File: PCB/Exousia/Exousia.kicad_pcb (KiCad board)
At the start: 2 copper layers, 72 parts, among them J1 IN/out, J2 I2C buss, J3 in/OUT, Q1 2N7002, Q2 2N7002, Q3 2N7002, U1 AON7410, U2 AON7410, U3 RVSPG, U4 AON7410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

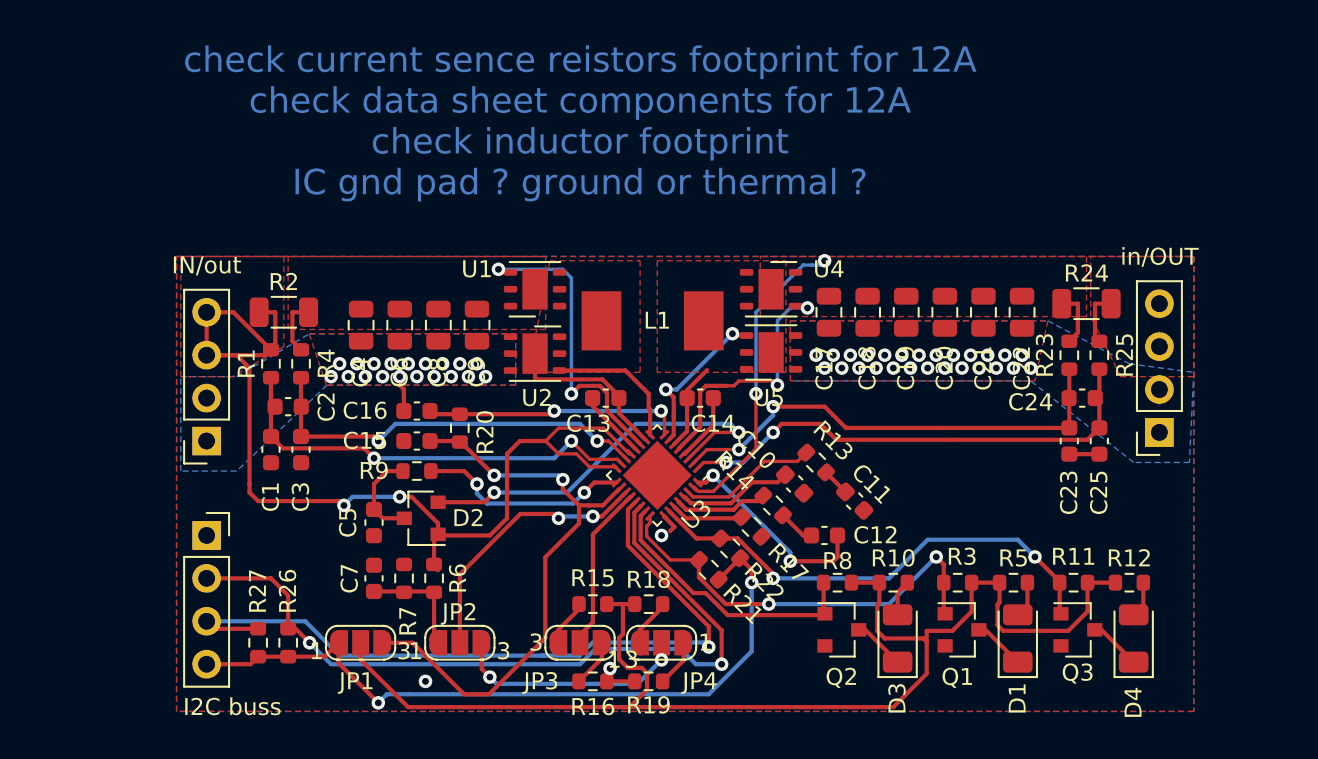
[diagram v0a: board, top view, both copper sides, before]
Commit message: upgraded sens resitors to handle 12A max. and retrouted a bit
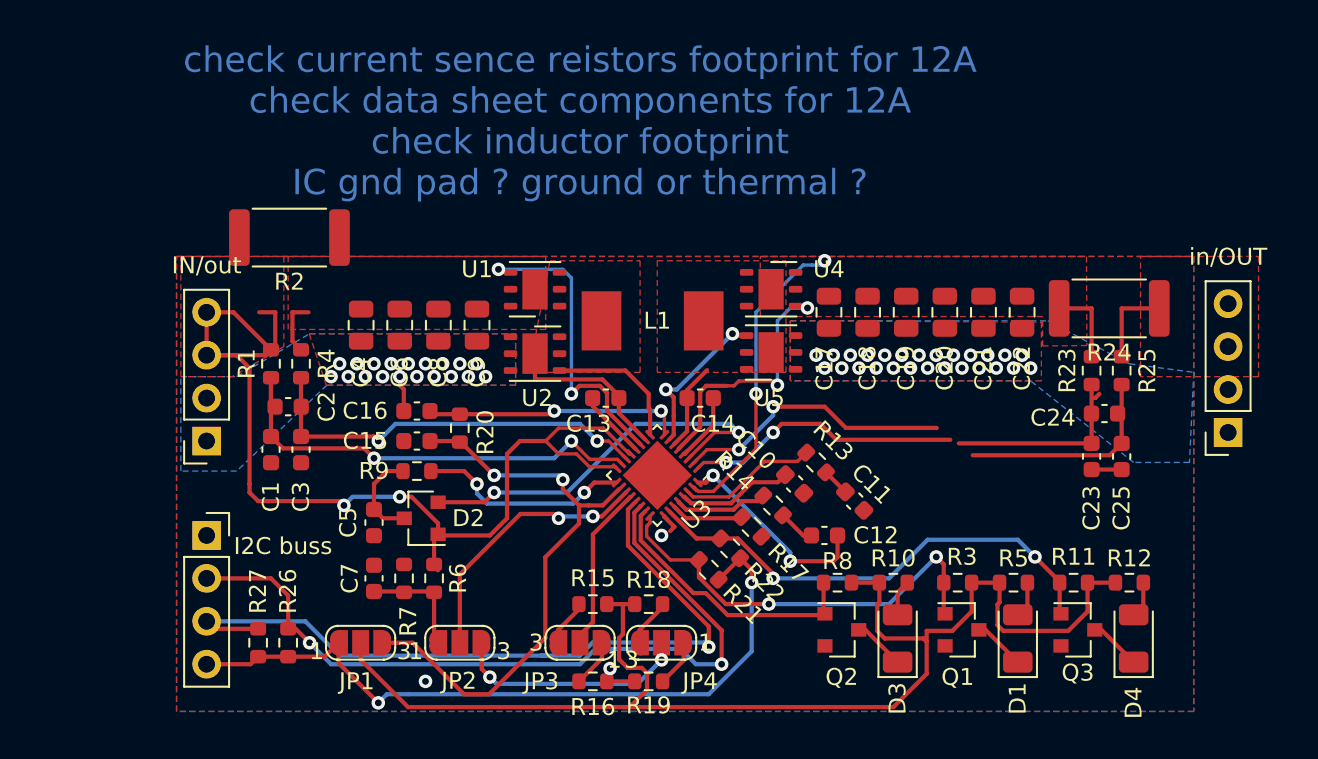
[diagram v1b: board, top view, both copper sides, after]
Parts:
- R2: value 0.02R -> 0.005R; footprint Resistor_SMD:R_1206_3216Metric -> Resistor_SMD:R_2512_6332Metric
- R24: value 0.01R -> 0.005R; footprint Resistor_SMD:R_1206_3216Metric -> Resistor_SMD:R_2512_6332Metric
- moved R2 4.43 mm to (138.3, 141.9)
- moved J3 4.06 mm to (193.8, 153.4)
- moved C25 1.61 mm to (187.5, 154.8)
- moved R25 1.61 mm to (187.5, 149.8)
- moved C23 1.61 mm to (185.7, 154.8)
- moved C24 1.61 mm to (186.5, 152.3)
- moved R23 1.61 mm to (185.7, 149.8)
- moved R24 1.37 mm to (186.8, 146.1)
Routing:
- net Net-(J3-Pad3): track 3.28 -> 5.08 mm
- net Net-(C17-Pad1): track 21.7 -> 23.1 mm

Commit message: improved the controle cirtitry for controleing the IC
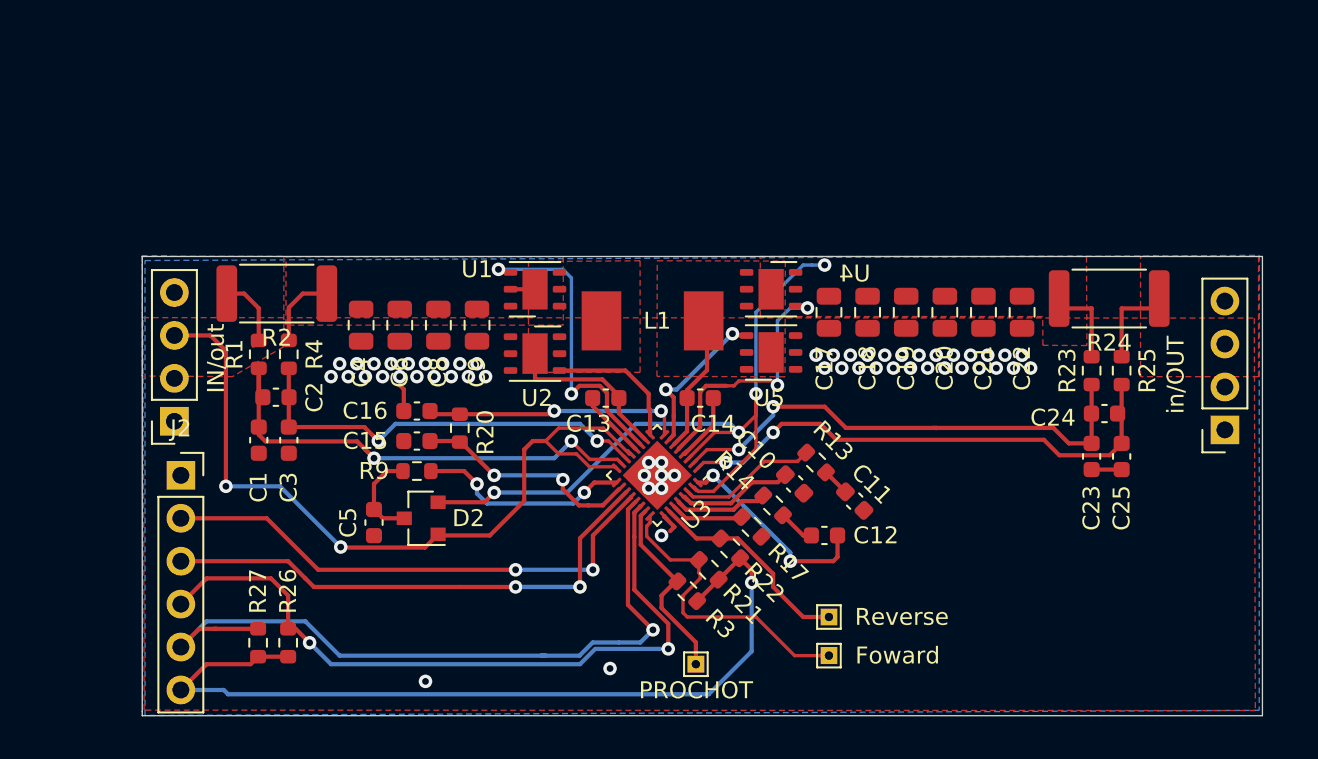
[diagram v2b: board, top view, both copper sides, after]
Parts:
- removed C7: 0.1uF, Capacitor_SMD:C_0603_1608Metric
- removed D1, D3: FRWPG, LED_SMD:LED_1206_3216Metric
- removed D4: RVSPG, LED_SMD:LED_1206_3216Metric
- removed JP1: IO-Vselect, Jumper:SolderJumper-3_P1.3mm_Open_RoundedPad1.0x1.5mm_NumberLabels
- removed JP2: Pin_FRWEN / ADP, Jumper:SolderJumper-3_P1.3mm_Open_RoundedPad1.0x1.5mm_NumberLabels
- removed JP3: RVSEN, Jumper:SolderJumper-3_P1.3mm_Open_RoundedPad1.0x1.5mm_NumberLabels
- removed JP4: Pin_FRWEN, Jumper:SolderJumper-3_P1.3mm_Open_RoundedPad1.0x1.5mm_NumberLabels
- removed Q1, Q2, Q3: 2N7002, Package_TO_SOT_SMD:SOT-23
- removed R10, R12, R15, R16, R18, R19, R5: 133K, Resistor_SMD:R_0603_1608Metric
- removed R11, R8: 10K, Resistor_SMD:R_0603_1608Metric
- removed R6: 402K, Resistor_SMD:R_0603_1608Metric
- removed R7: 135K, Resistor_SMD:R_0603_1608Metric
- added TP1: Foward, TestPoint:TestPoint_THTPad_1.0x1.0mm_Drill0.5mm, F.Cu at (170.2, 166.6)
- added TP2: Reverse, TestPoint:TestPoint_THTPad_1.0x1.0mm_Drill0.5mm, F.Cu at (170.2, 164.3)
- added TP3: PROCHOT, TestPoint:TestPoint_THTPad_1.0x1.0mm_Drill0.5mm, F.Cu at (162.3, 167.1)
- J2: value I2C buss -> Conn_01x06_Male; footprint Connector_PinSocket_2.54mm:PinSocket_1x04_P2.54mm_Vertical -> Connector_PinSocket_2.54mm:PinSocket_1x06_P2.54mm_Vertical
- R3: value 10K -> 3.3K
- U3: value RVSPG -> ISL95338
- moved R3 16.0 mm to (161.8, 162.8), turned to 135 degrees
- moved J2 3.87 mm to (131.8, 156.0)
- moved R2 3.40 mm to (137.5, 145.2)
- moved J1 2.23 mm to (131.4, 152.8)
- moved C1 0.91 mm to (136.4, 153.9)
- moved C2 0.91 mm to (137.5, 151.3)
- moved C3 0.91 mm to (138.2, 153.9)
- moved R1 0.91 mm to (136.4, 148.8)
- moved R4 0.91 mm to (138.2, 148.8)
- moved R24 0.58 mm to (186.8, 145.5)
- moved J3 0.24 mm to (193.6, 153.3)
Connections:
- net VDD renamed Net-(C15-Pad1)
- D2 pad 2: Net-(D2-Pad2) -> Net-(C17-Pad1)
- J2 pad 2: SCL -> RVSEN
- J2 pad 3: SDA -> Pin_FRWEN
- J2 pad 4: +3V3 -> SCL
- R3 pad 1: Net-(JP1-Pad2) -> +3V3
- R3 pad 2: FRWPG -> PROCHOT#
- U3 pad 19: Net-(JP2-Pad2) -> Pin_FRWEN
- U3 pad 3: Net-(D2-Pad2) -> Net-(C17-Pad1)
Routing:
- net Net-(JP1-Pad2): track 75.0 -> 0.00 mm
- net Net-(C17-Pad1): track 23.1 -> 48.8 mm, vias 2 -> 4
- net Net-(D2-Pad2): track 23.6 -> 0.00 mm, vias 2 -> 0
- net Net-(C15-Pad1): track 34.6 -> 13.4 mm
- net RVSEN: track 9.90 -> 30.9 mm, vias 0 -> 2
- net Net-(JP2-Pad2): track 16.9 -> 0.00 mm, vias 2 -> 0
- net Pin_FRWEN: track 14.2 -> 31.0 mm
- net RVSPG: track 28.8 -> 12.5 mm, vias 2 -> 0
- net Net-(D2-Pad1): track 61.4 -> 51.8 mm
- net +3V3: track 43.8 -> 51.5 mm, vias 2 -> 1
- net FRWPG: track 25.4 -> 18.2 mm, vias 2 -> 0
- net Net-(C7-Pad1): track 6.58 -> 0.00 mm
- net PROCHOT#: track 16.5 -> 11.4 mm
- net SCL: track 46.1 -> 42.6 mm
- net Net-(D4-Pad1): track 3.09 -> 0.00 mm
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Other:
- board outline added: 66.3 x 27.2 mm
- net class Default removed
- board text removed: "check current sence reistors footprint for 12A check data sheet components for 12A check inductor footprint IC gnd pad ? ground or thermal ?"
